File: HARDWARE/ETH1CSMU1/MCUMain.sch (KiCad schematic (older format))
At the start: 1 part

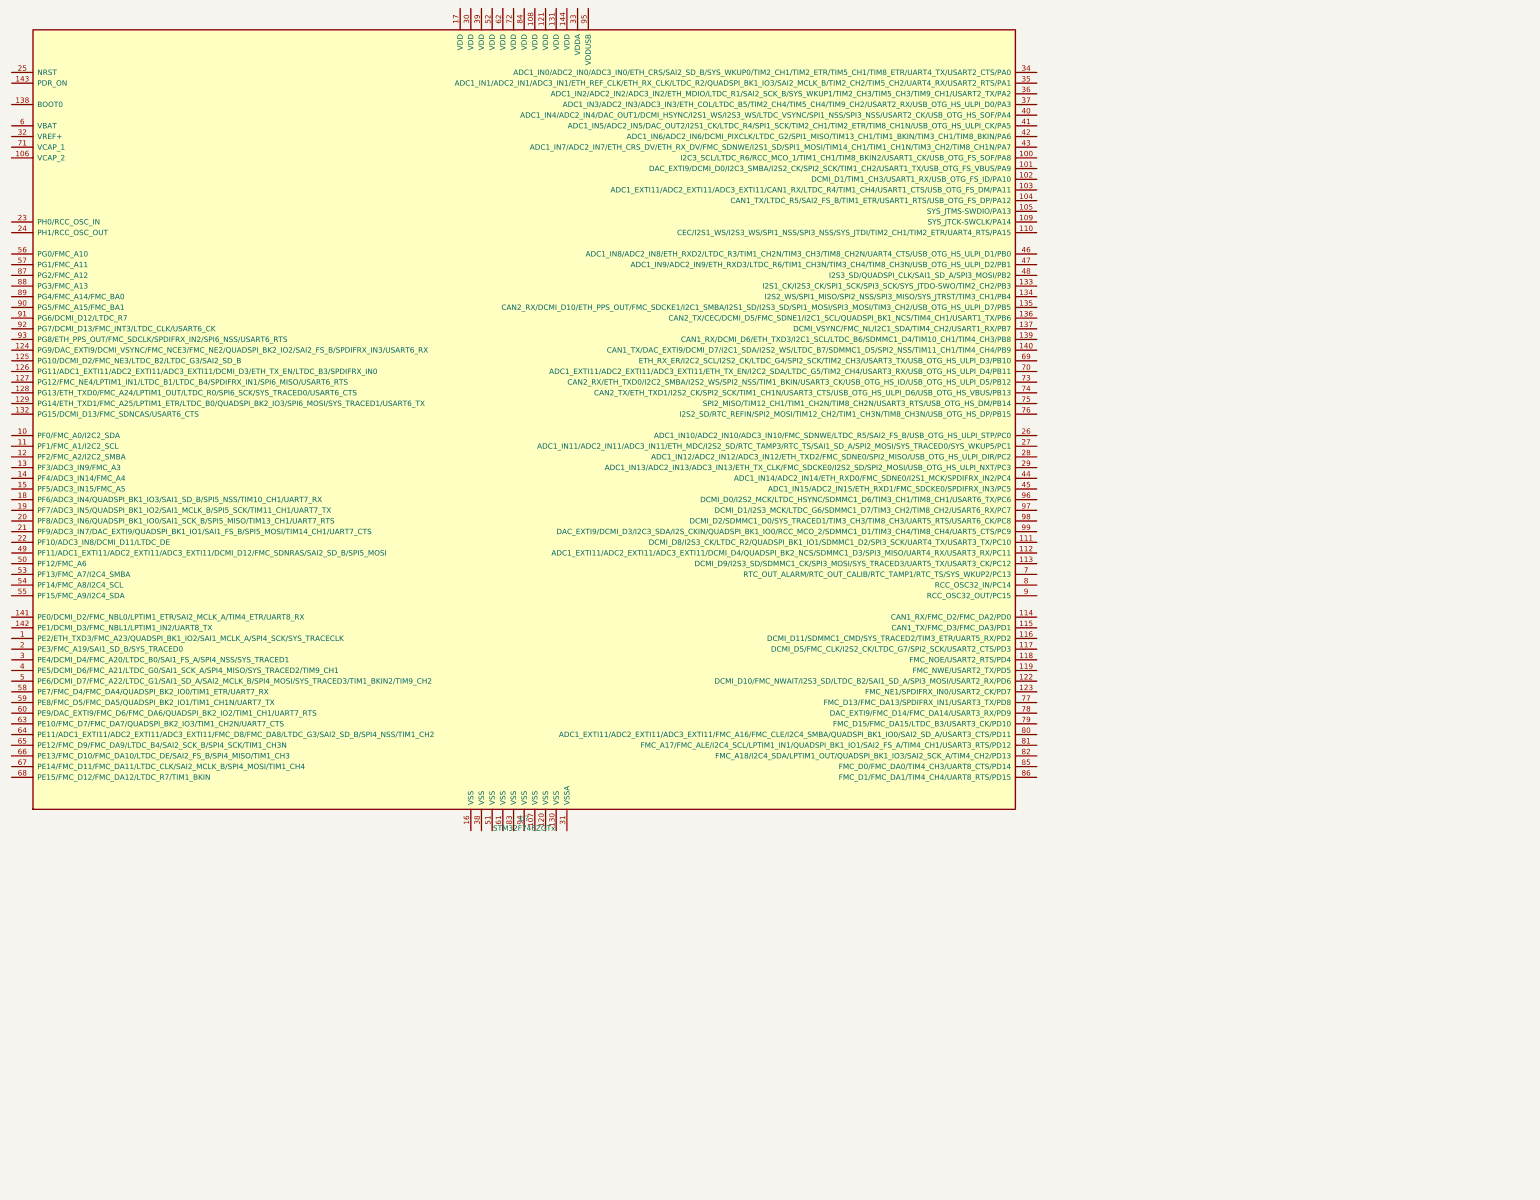
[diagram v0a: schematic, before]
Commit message: Added ADC
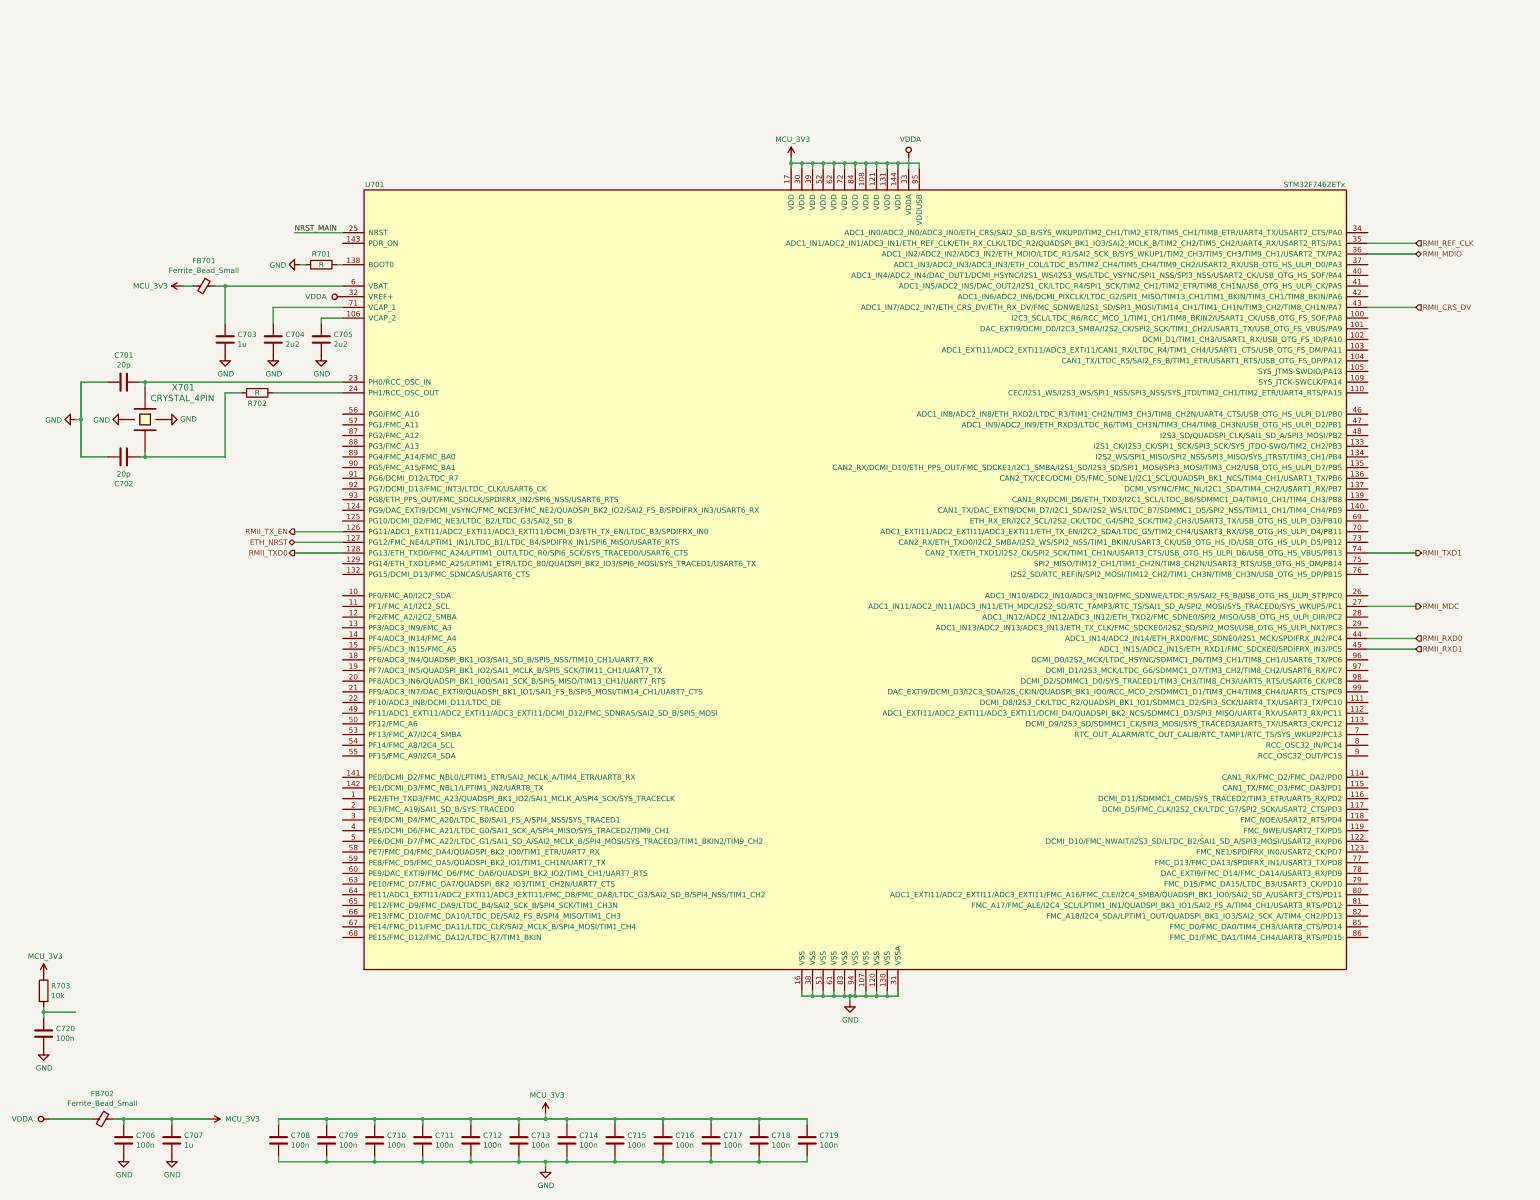
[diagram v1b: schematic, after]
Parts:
- removed U?: STM32F746ZGTx, Package_QFP:LQFP-144_20x20mm_P0.5mm, symbol MCU_ST_STM32F7:STM32F746ZGTx
- added C701, C702: 20p, symbol Device:C
- added C703, C707: 1u, symbol Device:C
- added C704, C705: 2u2, symbol Device:C
- added C706, C708, C709, C710, C711, C712, C713, C714, C715, C716, C717, C718, C719, C720: 100n, symbol Device:C
- added FB701, FB702: Ferrite_Bead_Small, symbol Device:Ferrite_Bead_Small
- added R701, R702: R, symbol Device:R
- added R703: 10k, symbol Device:R
- added U701: STM32F746ZETx, symbol stm32:STM32F746ZETx
- added X701: CRYSTAL_4PIN, symbol crystal_local:CRYSTAL_4PIN
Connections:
- new net: C705.1, U701.106 (VCAP_2)
- new net: R701.1, U701.138 (BOOT0)
- new net: C701.1, U701.23 (PH0/RCC_OSC_IN), X701.1
- new net: R702.1, U701.24 (PH1/RCC_OSC_OUT)
- new net: C703.1, FB701.1, U701.6 (VBAT)
- new net: C704.1, U701.71 (VCAP_1)
- new net: C702.2, R702.2, X701.3
- new net: C720.1, R703.2
- new net ETH_NRST: U701.127 (PG12/FMC_NE4/LPTIM1_IN1/LTDC_B1/LTDC_B4/SPDIFRX_IN1/SPI6_MISO/USART6_RTS)
- new net GND: C701.2, C702.1, C703.2, C704.2, C705.2, C706.2, C707.2, C708.2, C709.2, C710.2, C711.2, C712.2, C713.2, C714.2, C715.2, C716.2, C717.2, C718.2, C719.2, C720.2, R701.2, U701.107 (VSS), U701.120 (VSS), U701.130 (VSS), U701.16 (VSS), U701.31 (VSSA), U701.38 (VSS), U701.51 (VSS), U701.61 (VSS), U701.83 (VSS), U701.94 (VSS), X701.2 (GND), X701.4 (GND)
- new net MCU_3V3: C706.1, C707.1, C708.1, C709.1, C710.1, C711.1, C712.1, C713.1, C714.1, C715.1, C716.1, C717.1, C718.1, C719.1, FB701.2, FB702.1, R703.1, U701.108 (VDD), U701.121 (VDD), U701.131 (VDD), U701.144 (VDD), U701.17 (VDD), U701.30 (VDD), U701.39 (VDD), U701.52 (VDD), U701.62 (VDD), U701.72 (VDD), U701.84 (VDD), U701.95 (VDDUSB)
- new net NRST_MAIN: U701.25 (NRST)
- new net RMII_CRS_DV: U701.43 (ADC1_IN7/ADC2_IN7/ETH_CRS_DV/ETH_RX_DV/FMC_SDNWE/I2S1_SD/SPI1_MOSI/TIM14_CH1/TIM1_CH1N/TIM3_CH2/TIM8_CH1N/PA7)
- new net RMII_MDC: U701.27 (ADC1_IN11/ADC2_IN11/ADC3_IN11/ETH_MDC/I2S2_SD/RTC_TAMP3/RTC_TS/SAI1_SD_A/SPI2_MOSI/SYS_TRACED0/SYS_WKUP5/PC1)
- new net RMII_MDIO: U701.36 (ADC1_IN2/ADC2_IN2/ADC3_IN2/ETH_MDIO/LTDC_R1/SAI2_SCK_B/SYS_WKUP1/TIM2_CH3/TIM5_CH3/TIM9_CH1/USART2_TX/PA2)
- new net RMII_REF_CLK: U701.35 (ADC1_IN1/ADC2_IN1/ADC3_IN1/ETH_REF_CLK/ETH_RX_CLK/LTDC_R2/QUADSPI_BK1_IO3/SAI2_MCLK_B/TIM2_CH2/TIM5_CH2/UART4_RX/USART2_RTS/PA1)
- new net RMII_RXD0: U701.44 (ADC1_IN14/ADC2_IN14/ETH_RXD0/FMC_SDNE0/I2S1_MCK/SPDIFRX_IN2/PC4)
- new net RMII_RXD1: U701.45 (ADC1_IN15/ADC2_IN15/ETH_RXD1/FMC_SDCKE0/SPDIFRX_IN3/PC5)
- new net RMII_TXD0: U701.128 (PG13/ETH_TXD0/FMC_A24/LPTIM1_OUT/LTDC_R0/SPI6_SCK/SYS_TRACED0/USART6_CTS)
- new net RMII_TXD1: U701.74 (CAN2_TX/ETH_TXD1/I2S2_CK/SPI2_SCK/TIM1_CH1N/USART3_CTS/USB_OTG_HS_ULPI_D6/USB_OTG_HS_VBUS/PB13)
- new net RMII_TX_EN: U701.126 (PG11/ADC1_EXTI11/ADC2_EXTI11/ADC3_EXTI11/DCMI_D3/ETH_TX_EN/LTDC_B3/SPDIFRX_IN0)
- new net VDDA: FB702.2, U701.32 (VREF+), U701.33 (VDDA)

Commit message: Commit
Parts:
- added J701: Conn_02x05, symbol Connector_Generic:Conn_02x05_Odd_Even
- added R704, R705: 4k7, symbol Device:R
- added U702: 24LC08, symbol Memory_EEPROM:24LC08
- C708, C709, C710, C711, C712, C713, C714, C715, C716, C717, C718, C719, C720: footprint (none) -> SMD:C_0603_Symbol1
- FB701, FB702: value Ferrite_Bead_Small -> MPZ2012S221A; footprint (none) -> SMD:R_0805_Symbol1
- R703: footprint (none) -> SMD:R_0603_Symbol1
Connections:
- net GND: now also J701.3 (Pin_3), J701.5 (Pin_5), U702.1 (A0), U702.2 (A1), U702.3 (A2), U702.4 (GND), U702.7 (WP)
- net MCU_3V3: now also J701.1 (Pin_1), R704.1, R705.1, U702.8 (VCC)
- net CAN_STBY: now reaches U701.102 (DCMI_D1/TIM1_CH3/USART1_RX/USB_OTG_FS_ID/PA10)
- net CAN1_RX: now reaches U701.103 (ADC1_EXTI11/ADC2_EXTI11/ADC3_EXTI11/CAN1_RX/LTDC_R4/TIM1_CH4/USART1_CTS/USB_OTG_FS_DM/PA11)
- net CAN1_TX: now reaches U701.104 (CAN1_TX/LTDC_R5/SAI2_FS_B/TIM1_ETR/USART1_RTS/USB_OTG_FS_DP/PA12)
- net MAIN-SWDIO-TMS: now reaches U701.105 (SYS_JTMS-SWDIO/PA13)
- net MAIN-SWDIO-TMS: now also J701.2 (Pin_2)
- net MAIN-SWDCKL-TCK: now reaches U701.109 (SYS_JTCK-SWCLK/PA14)
- net MAIN-SWDCKL-TCK: now also J701.4 (Pin_4)
- net MAIN-NC-TDI: now reaches U701.110 (CEC/I2S1_WS/I2S3_WS/SPI1_NSS/SPI3_NSS/SYS_JTDI/TIM2_CH1/TIM2_ETR/UART4_RTS/PA15)
- net MAIN-NC-TDI: now also J701.8 (Pin_8)
- net MAIN-SWO-TDO: now reaches U701.133 (I2S1_CK/I2S3_CK/SPI1_SCK/SPI3_SCK/SYS_JTDO-SWO/TIM2_CH2/PB3)
- net MAIN-SWO-TDO: now also J701.6 (Pin_6)
- new net MAIN-I2C1_SCL: R705.2, U702.6 (SCL)
- new net MAIN-I2C1_SDA: R704.2, U702.5 (SDA)
- new net MAIN-NRST: J701.10 (Pin_10)
- no-connect marks 0 -> 2
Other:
- moved on the sheet: C701, C702, C720, R702, R703, X701
